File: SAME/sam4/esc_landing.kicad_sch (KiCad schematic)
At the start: 11 parts, among them M1 MR30PW-FB, M2 MR30PW-FB, M3 MR30PW-FB, M4 MR30PW-FB, U2 T-motor_F55A_PROII, U3 BM10B-SRSS-TB, U9 BM10B-SRSS-TB

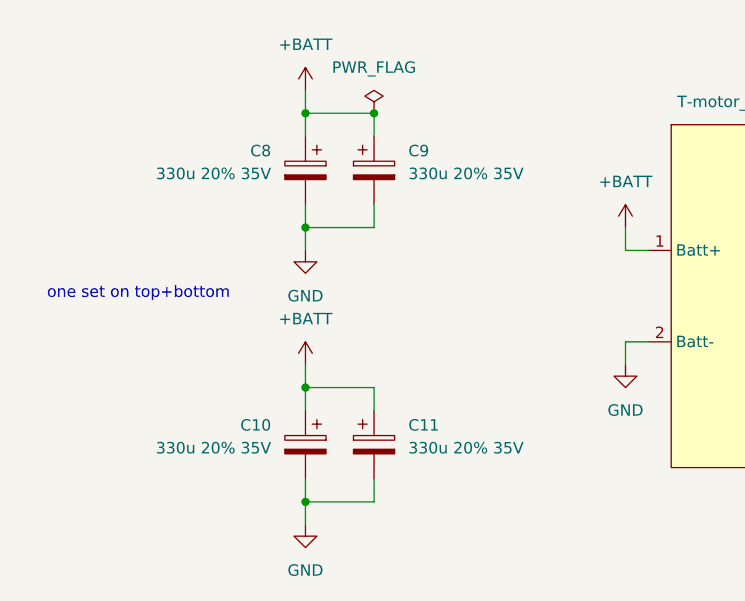
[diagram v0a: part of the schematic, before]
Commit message: add JLC ordering files. small tweaks
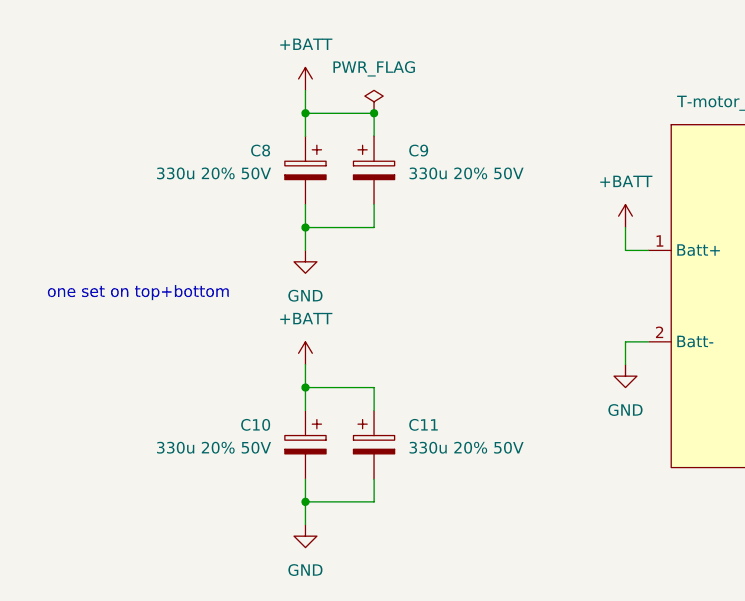
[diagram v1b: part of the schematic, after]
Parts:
- C10, C11, C8, C9: value 330u 20% 35V -> 330u 20% 50V; LCSC (none) -> C249985
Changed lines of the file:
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@@
 			)
 		)
-		(property "Value" "330u 20% 35V"
+		(property "Value" "330u 20% 50V"
 			(at 44.45 114.6809 0)
 			(effects
@@
 			)
 		)
-		(property "LCSC" ""
+		(property "LCSC" "C249985"
 			(at 48.26 114.3 0)
 			(effects
@@
 			)
 		)
-		(property "Value" "330u 20% 35V"
+		(property "Value" "330u 20% 50V"
 			(at 59.69 84.2009 0)
 			(effects
@@
 			)
 		)
-		(property "LCSC" ""
+		(property "LCSC" "C249985"
 			(at 55.88 83.82 0)
 			(effects
@@
 			)
 		)
-		(property "Value" "330u 20% 35V"
+		(property "Value" "330u 20% 50V"
 			(at 59.69 114.6809 0)
 			(effects
@@
 			)
 		)
-		(property "LCSC" ""
+		(property "LCSC" "C249985"
 			(at 55.88 114.3 0)
 			(effects
@@
 			)
 		)
-		(property "Value" "330u 20% 35V"
+		(property "Value" "330u 20% 50V"
 			(at 44.45 84.2009 0)
 			(effects
@@
 			)
 		)
-		(property "LCSC" ""
+		(property "LCSC" "C249985"
 			(at 48.26 83.82 0)
 			(effects
